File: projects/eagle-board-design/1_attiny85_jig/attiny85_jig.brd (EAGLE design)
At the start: 36 x 12 mm, 10 parts, among them IC2 LIPO_CHARGER/OT

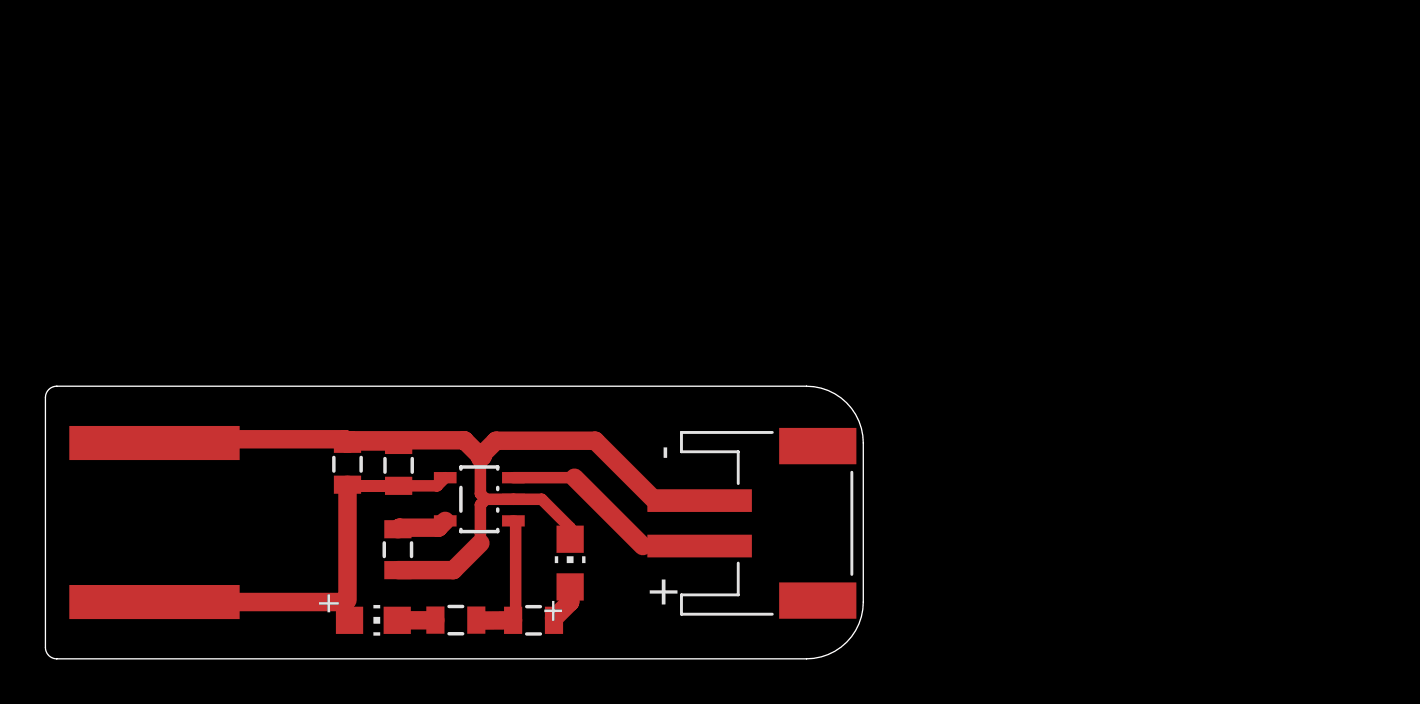
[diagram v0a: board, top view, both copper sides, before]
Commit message: adds board design intro files; increases attiny85 bent leg size
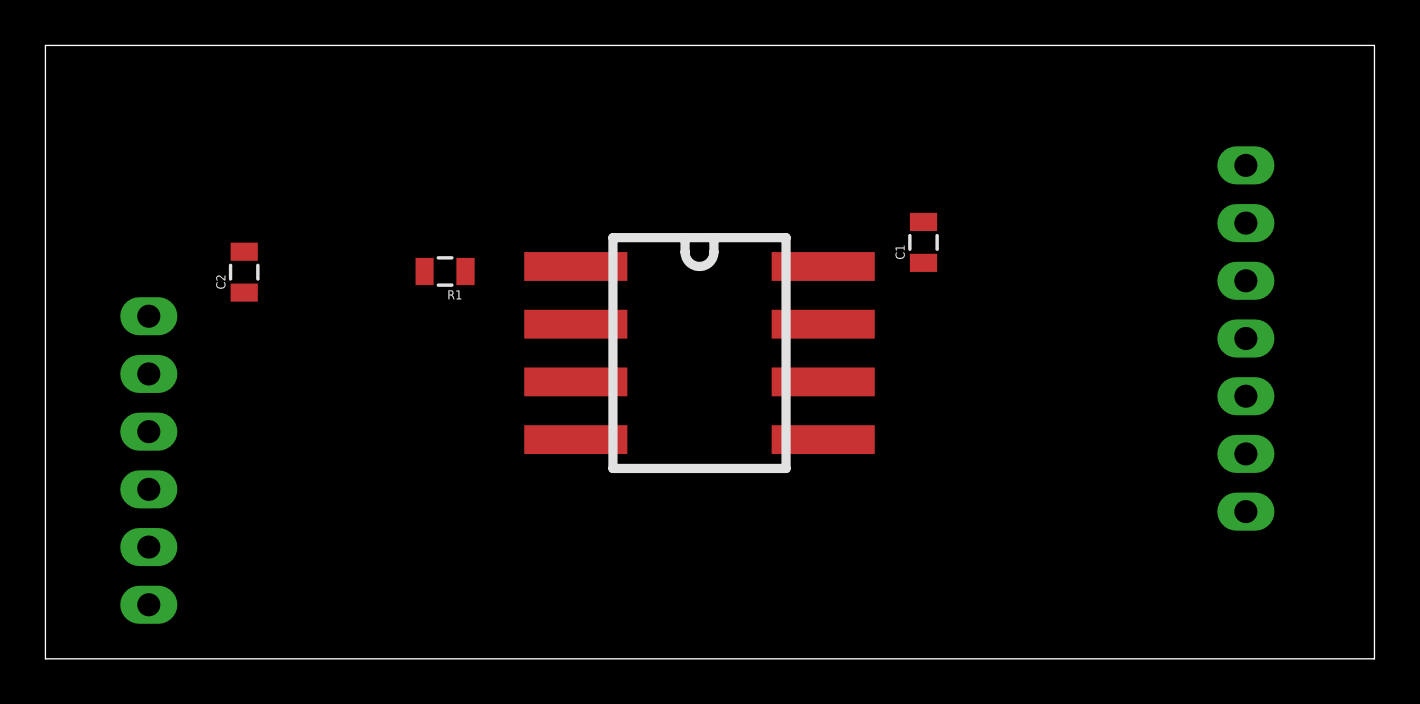
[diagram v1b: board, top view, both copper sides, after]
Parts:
- removed CN1: (no value), homemade-hardware:JST-PH-2-SMT-RA
- removed IC2: LIPO_CHARGER/OT, homemade-hardware:SOT23-5L
- removed LED1: RED-2V/20mA, homemade-hardware:CHIP-LED0805
- removed LED2: GREEN-2V/20mA, homemade-hardware:CHIP-LED0805
- removed R2, R3: 150, homemade-hardware:0805
- added U$1: ATTINY85-SOCKET-BENT, homemade-hardware:SOCKET-8PIN-BENT
- added U$3: HEADER-7, homemade-hardware:HEADER-7
- C1: value 10uF -> 0.1uF
- C2: value 0.1uF -> 10uF
- U$2: value USB-PCB-POWER -> HEADER-6; device homemade-hardware:USB-A-PCB-POWER -> homemade-hardware:HEADER-6
- moved C1 27.2 mm to (38.6, 18.3)
- moved R1 12.4 mm to (17.6, 17.1), turned to 180 degrees
- moved C2 10.9 mm to (8.75, 17.0)
- moved U$2 3.65 mm to (4.55, 2.38)
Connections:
- removed net BATTERY: CN1.1, IC2.3
- removed net CURRENT-CONTROL: IC2.5, R1.2
- removed net STATUS: IC2.1, R2.1, R3.2
- new net N$1: U$1.5, U$3.4
- new net N$4: C2.1, U$2.6
- new net RESET: R1.1, U$1.1, U$3.5
- net 5V: now also R1.2, U$1.8, U$2.4; no longer C2.1, IC2.4, LED1.A, U$2.5V
- net GND: now also U$1.4, U$2.3; no longer CN1.2, IC2.2, LED2.C, R1.1, U$2.GND
- net N$2: now also U$1.6, U$3.3; no longer LED1.C, R2.2
- net N$3: now also U$1.7, U$3.2; no longer LED2.A, R3.1
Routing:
- net GND: track 41.2 -> 0.00 mm
- net 5V: track 21.3 -> 0.00 mm
- net BATTERY: track 9.44 -> 0.00 mm
- net STATUS: track 6.09 -> 0.00 mm
- net CURRENT-CONTROL: track 2.24 -> 0.00 mm
- net N$3: track 1.77 -> 0.00 mm
- net N$2: track 1.69 -> 0.00 mm
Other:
- board size 36 x 12 mm -> 58.5 x 27 mm

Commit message: gives names to connections in jig pcb
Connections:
- net N$1 renamed MOSI
- net N$2 renamed MISO
- net N$3 renamed SCK
- net N$4 renamed ARDUINO_RESET
- net RESET renamed TINY_RESET
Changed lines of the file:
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@@
 </elements>
 <signals>
-<signal name="RESET">
+<signal name="TINY_RESET">
 <contactref element="U$1" pad="1"/>
 <contactref element="U$3" pad="5"/>
@@
 <wire x1="18.49" y1="17.05" x2="23.345" y2="17.27" width="0" layer="19" extent="1-1"/>
 </signal>
-<signal name="N$1">
+<signal name="MOSI">
 <contactref element="U$1" pad="5"/>
 <contactref element="U$3" pad="4"/>
 <wire x1="34.235" y1="9.65" x2="52.84" y2="14.1" width="0" layer="19" extent="1-1"/>
 </signal>
-<signal name="N$2">
+<signal name="MISO">
 <contactref element="U$1" pad="6"/>
 <contactref element="U$3" pad="3"/>
 <wire x1="34.235" y1="12.19" x2="52.84" y2="16.64" width="0" layer="19" extent="1-1"/>
 </signal>
-<signal name="N$3">
+<signal name="SCK">
 <contactref element="U$1" pad="7"/>
 <contactref element="U$3" pad="2"/>
 <wire x1="34.235" y1="14.73" x2="52.84" y2="19.18" width="0" layer="19" extent="1-1"/>
 </signal>
-<signal name="N$4">
+<signal name="ARDUINO_RESET">
 <contactref element="U$2" pad="6"/>
 <contactref element="C2" pad="1"/>
